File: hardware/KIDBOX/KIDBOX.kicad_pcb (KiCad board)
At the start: 2 copper layers, 155 x 75 mm, 22 parts, among them J1 RP2350-Plus 1-20, J2 RP2350-Plus 21-40, J3 TFT ILI9341 2.4in, J5 DAC GY-PCM5102, SW1 DOWN, SW10 ON/OFF, SW2 LEFT, SW3 UP, SW4 RIGHT, SW5 SELECT, SW6 START, SW7 B, SW8 A

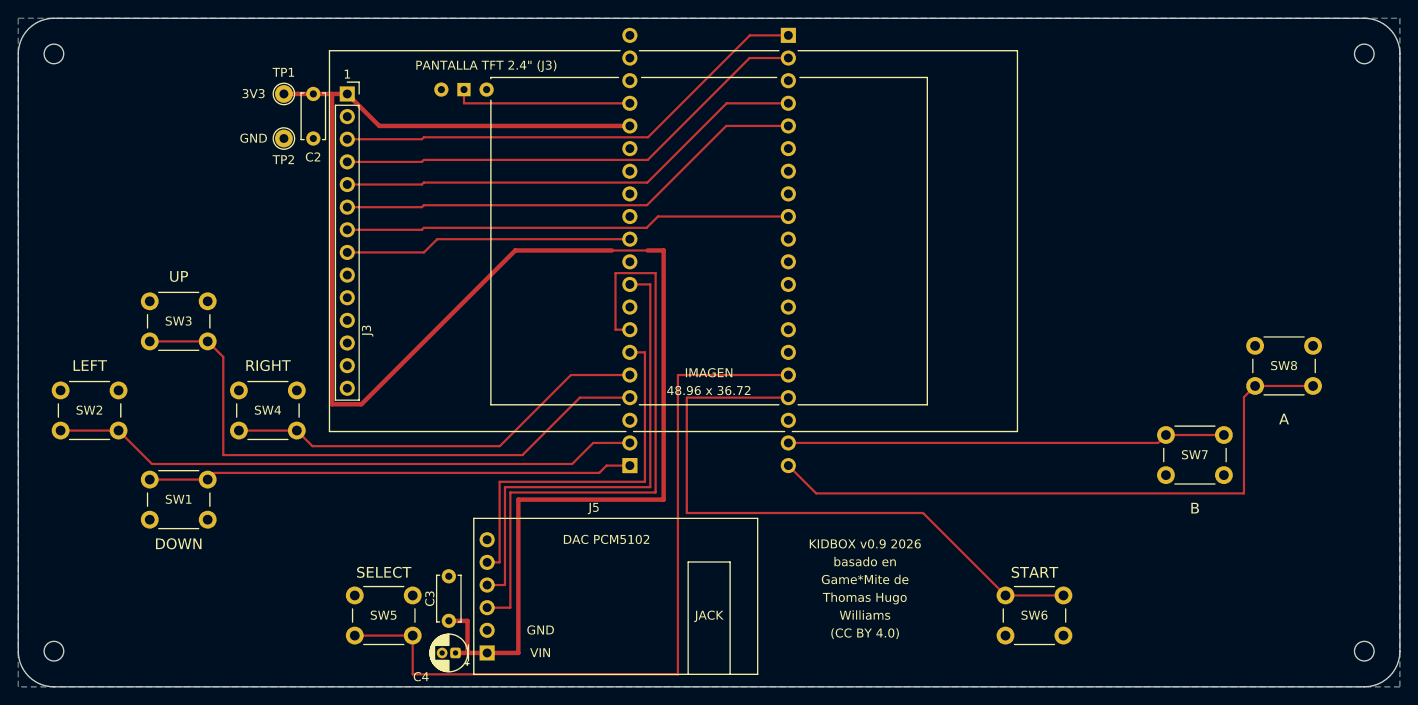
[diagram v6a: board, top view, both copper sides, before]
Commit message: v0.9: 150x70, controles Ø9, muro DAC-pantalla, batería en carcasa
Ajuste tras la prueba 1:1 (mismo PR #27):
- Placa 150 x 70 (r = 4), agujeros M2 en (4,4), (146,4), (4,66), (146,66); eje de simetría x = 75.
- Imagen centrada en x = 75: módulo x 32.41-109.59, J3 en x = 34.41. RP2350-Plus en 66.11 / 83.89.
- Controles compactos con capuchones Ø9: cruceta (16.5, 39) con brazos de 9 mm, A (138, 34.5), B (129, 43.5),
  SELECT/START (38.5, 62) / (111.5, 62). UP entra por el borde izquierdo (entre columnas quedan 0.5 mm).
- DAC 5 mm más arriba: J5 en x = 50.1 (VIN y = 66.2), jack con eje en x = 75 y boca en y = 70; C3/C4 junto a VIN.
- Franja de 4.74 mm para un muro colgante de la carcasa entre pantalla y DAC (línea en F.Fab).
- Batería en la carcasa: zona solo de referencia en B.SilkS con flecha al conector BAT; patas THT permitidas.
- SW10 en (47.5, 8); TP1/TP2 junto a C2.
- ESPECIFICACION.md (v0.9 + ajuste), DECISIONES.md sección 17, README (carcasa), BOM_compra (Ø9, sujeción en carcasa).

verificar.py: SIN ERRORES (ERC 0/0, DRC 0/0, sin conectar 0, paridad 0).
verificar_extra.py: 0 con los tests ignorados activados; F8 en seco 0 cambios.

Co-Authored-By: Claude Opus 5.5 <noreply@anthropic.com>
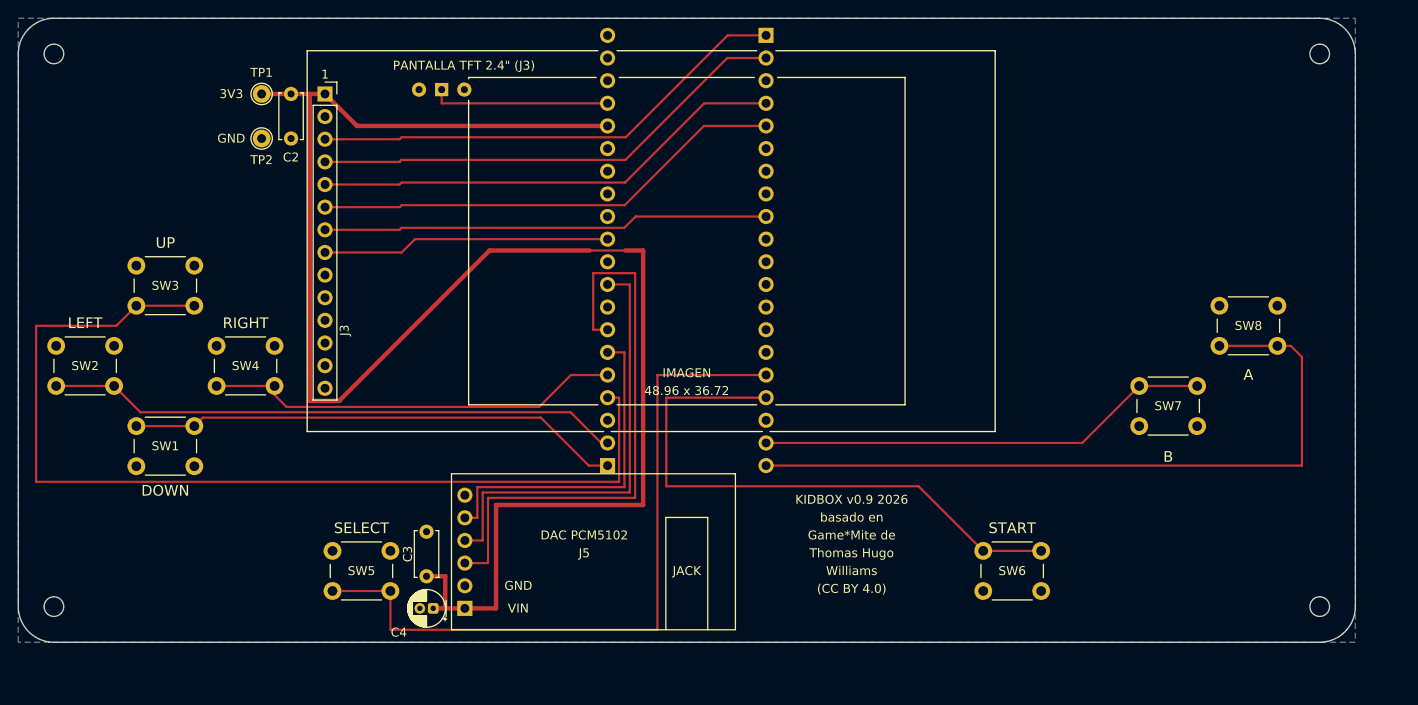
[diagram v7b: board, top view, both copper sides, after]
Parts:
- moved H4 7.07 mm to (146.0, 66.0)
- moved SW7 6.26 mm to (125.8, 41.2)
- moved SW1 6.18 mm to (13.2, 45.8)
- moved SW8 6.02 mm to (141.2, 36.8)
- moved C4 5.59 mm to (46.5, 66.2)
- moved J5 5.59 mm to (50.1, 66.2)
- moved SW4 5.59 mm to (28.8, 41.2)
- moved SW5 5.59 mm to (41.8, 64.2)
- moved SW6 5.59 mm to (108.2, 59.8)
- moved C3 5.59 mm to (45.8, 62.6)
- moved SW2 5.02 mm to (10.8, 41.2)
- moved H2 5.00 mm to (146.0, 4.00)
- moved H3 5.00 mm to (4.00, 66.0)
- moved SW3 4.27 mm to (19.8, 32.2)
- moved C2 2.50 mm to (30.6, 8.49)
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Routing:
- net /BTN_UP: track 68.3 -> 112.3 mm
- net /BTN_A: track 71.5 -> 82.1 mm
- net +3V3: track 193.7 -> 188.5 mm
- net /BTN_SELECT: track 86.6 -> 81.6 mm
- net /I2S_LRCK: track 68.9 -> 64.3 mm
- net /I2S_DIN: track 54.3 -> 49.7 mm
- net /I2S_BCK: track 42.9 -> 38.4 mm
- net /BTN_START: track 70.4 -> 66.2 mm
- net /BTN_LEFT: track 66.4 -> 64.5 mm
- net /BTN_B: track 49.2 -> 51.0 mm
- net /BTN_RIGHT: track 47.9 -> 46.9 mm
- net /BTN_DOWN: track 54.5 -> 55.5 mm
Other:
- board size 155 x 75 mm -> 150 x 70 mm
- board text added: "150 x 70 mm - 1.6 mm - 2 capas"
- board text added: "BAT"
- board text added: "muro carcasa (colgante, termina >= 4 mm sobre la PCB; ancho ~ 2 mm)"
- board text added: "va en la carcasa, no pegar a la PCB"
- board text removed: "155 x 75 mm - 1.6 mm - 2 capas"
- board text removed: "sin patas THT"

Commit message: v1.0: pistas a 45°, prueba 1:1, versión de fabricación
Revisión 2 del profesor:
- gen_pcb.py reemplaza cada codo a 90° por un chaflán a 45° (d = 1.0 mm, o largo/2; menor si hace falta para
  0.29 mm a pads y 0.30 mm a pistas). Esquinas a 90°: 33 -> 0 (112 a 45°, 3 colineales). Sin mover huellas.
- verificar_extra.py cuenta las esquinas de pista y falla si queda alguna a 90°.
- Prueba 1:1 de la 150 x 70 (27-oct): fotos en KIDBOX/verificacion/, pendiente cerrado; BOM_compra con un
  100 nF más de repuesto (C2 perdido); README: batería con el cable hacia el conector BAT.
- Versión de fabricación v1.0: serigrafía, cajetín, ESPECIFICACION, README (sin PRELIMINAR), zip
  KIDBOX_gerbers_v1.0.zip y carpeta de entrega. DECISIONES.md sección 18.

verificar.py: SIN ERRORES (ERC 0/0, DRC 0/0, sin conectar 0, paridad 0).
verificar_extra.py: 0 con los tests ignorados activados; F8 en seco 0 cambios; 0 esquinas a 90°.

Co-Authored-By: Claude Opus 5.5 <noreply@anthropic.com>
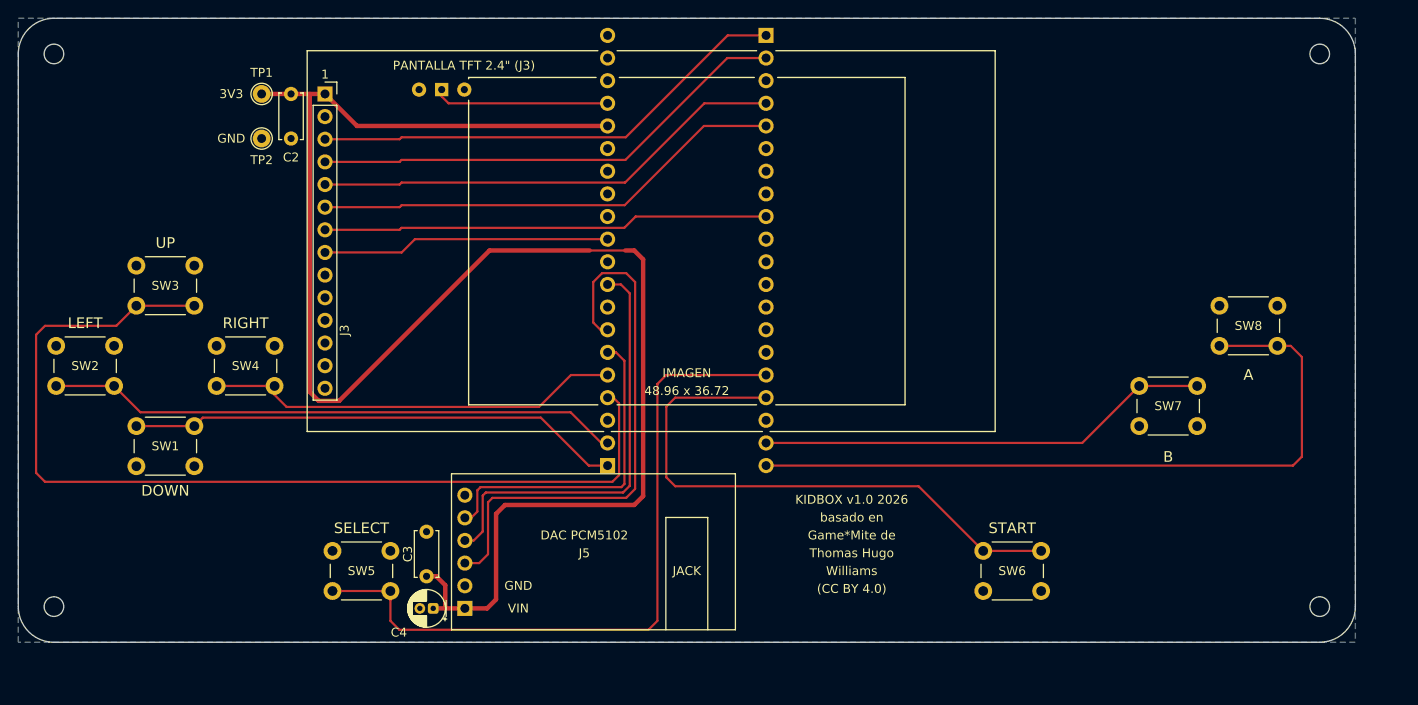
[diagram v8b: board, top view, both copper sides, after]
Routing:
- net +3V3: track 188.5 -> 185.0 mm
- net /I2S_LRCK: track 64.3 -> 61.2 mm
- net /BTN_SELECT: track 81.6 -> 79.2 mm
- net /BTN_UP: track 112.3 -> 110.3 mm
- net /I2S_DIN: track 49.7 -> 47.9 mm
- net /I2S_BCK: track 38.4 -> 37.0 mm
- net /BTN_START: track 66.2 -> 65.0 mm
- net /BTN_A: track 82.1 -> 81.5 mm
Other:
- board text added: "KIDBOX v1.0 - 27-oct-2026"
- board text added: "KIDBOX v1.0 2026"
- board text removed: "KIDBOX v0.9 - 26-oct-2026"
- board text removed: "KIDBOX v0.9 2026"
